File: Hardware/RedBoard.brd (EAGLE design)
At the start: 68.6 x 54.4 mm, 54 parts, among them IC1 FT232RLSSOP, IC2 LMV358, IC3 LM1117, J1 ICSP, J4 POWER_JACKSMD, Q1 MOSFET-PCHANNELSMD, U2 MIC5205, U3 ATMEGA328, Y1 16MHz

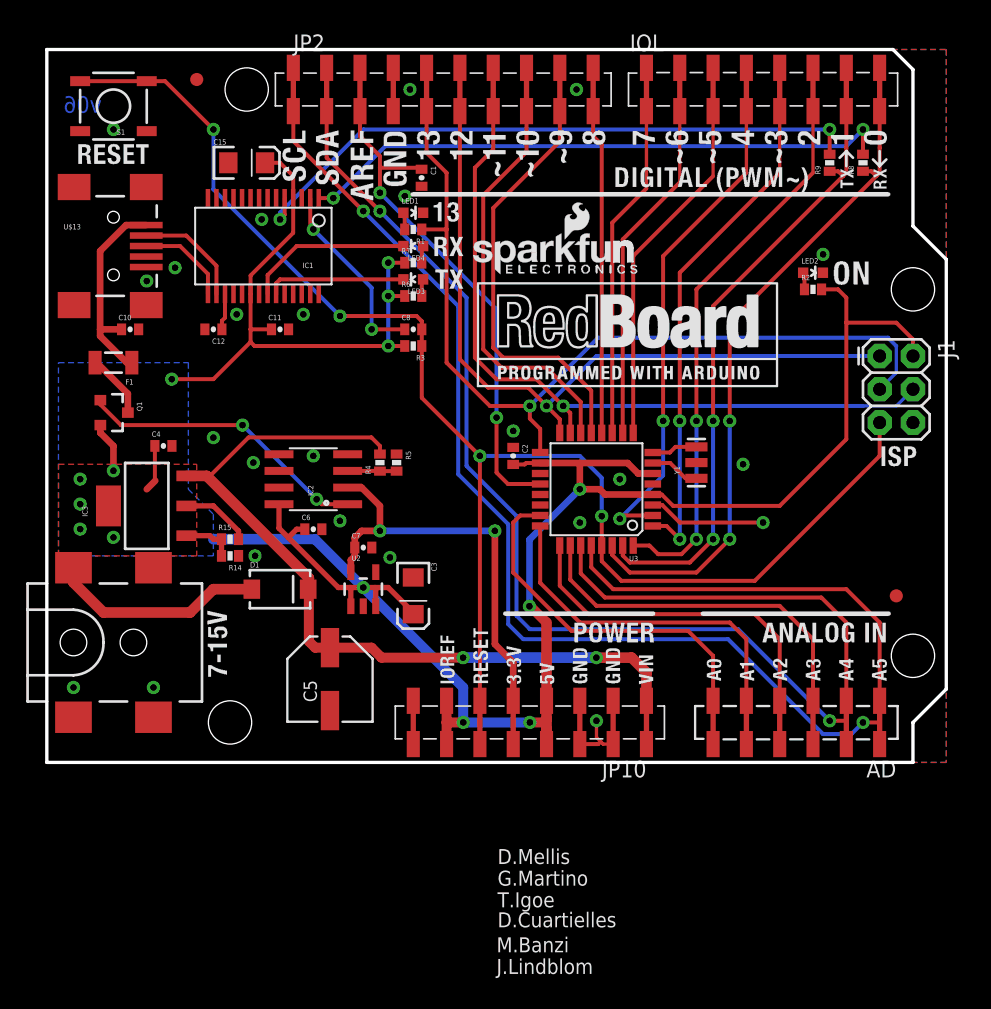
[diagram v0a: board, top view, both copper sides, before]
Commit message: New SMD ICSP header, logo, FT231X, power select
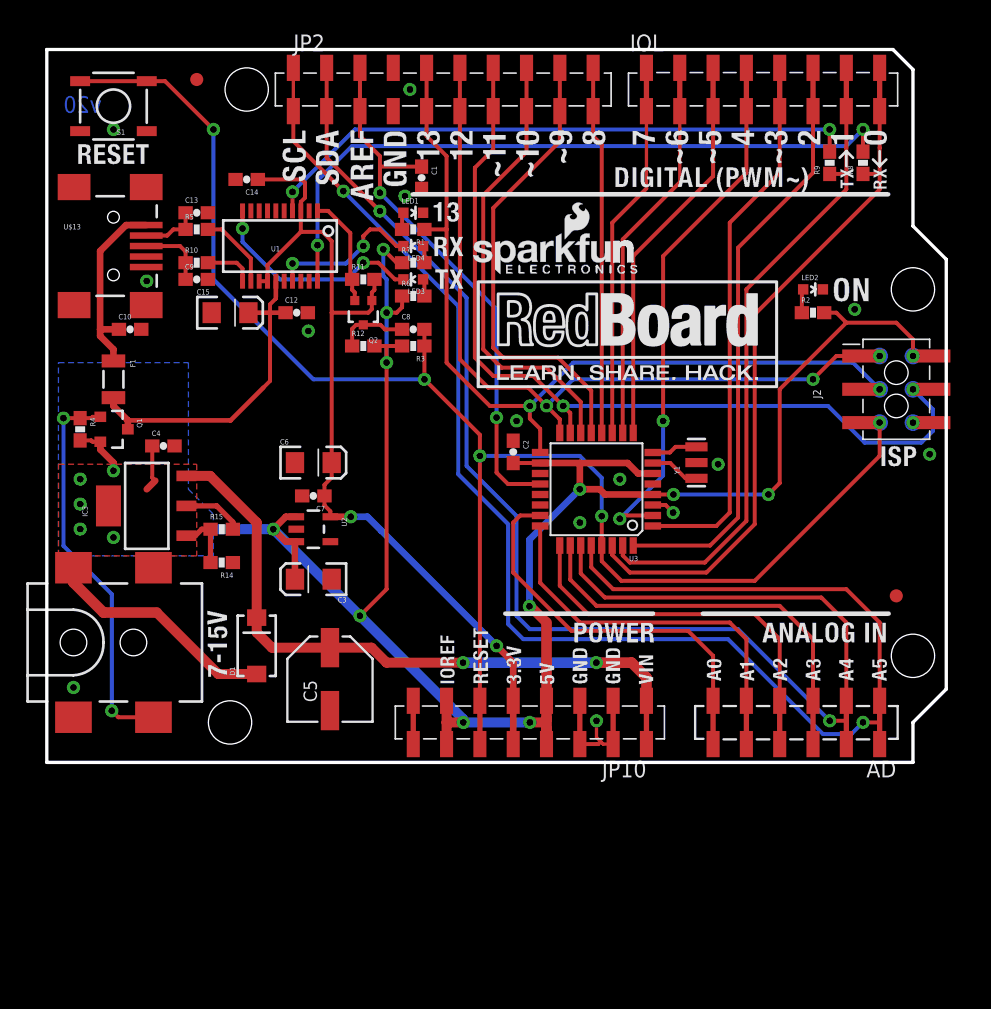
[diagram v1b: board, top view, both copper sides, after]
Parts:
- removed C11: 0.1uF, SparkFun-Capacitors:0402-CAP
- removed IC1: FT232RLSSOP, SparkFun-DigitalIC:SSOP28DB
- removed IC2: LMV358, SparkFun:SO08
- removed J1: ICSP, SparkFun:2X3
- removed U$15: CREATIVE_COMMONS, SparkFun:CREATIVE_COMMONS
- added C13, C9: 47pF, SparkFun-Capacitors:0603-CAP
- added C14: 0.1uF, SparkFun:0603-CAP
- added FRAME2: FRAME-LETTER, SparkFun-Aesthetics:CREATIVE_COMMONS
- added J2: AVR_SPI_PRG_6SMT_MALE, SparkFun-Connectors:2X3_SMT_POSTS
- added Q2: 2N7002PW, SparkFun-DiscreteSemi:SOT323
- added R10: 27, SparkFun-Resistors:0603-RES
- added R11, R12: 10k, SparkFun:0603-RES
- added TP1, TP2, TP3, TP4, TP5, TP6: TP-3x5, SparkFun-Passives:PAD.03X.05
- added U1: FT231XS, SparkFun-DigitalIC:SSOP20_L
- C1, C10, C12, C2, C4, C7, C8: device SparkFun:0402-CAP -> SparkFun:0603-CAP
- C6: value 0.1uF -> 10uF; device SparkFun:0402-CAP -> SparkFun:EIA3216
- JP2: value M10SMD -> M10SMD_COMBO
- Q1: value MOSFET-PCHANNELSMD -> ZXMP6A13FTA
- R1, R14, R15, R2, R3, R4, R6, R7, R8, R9: device SparkFun:0402-RES -> SparkFun:0603-RES
- R5: value 10k -> 27; device SparkFun:0402-RES -> SparkFun-Resistors:0603-RES
- moved R5 23.4 mm to (11.4, 40.6), turned to 0 degrees
- moved R4 23.0 mm to (2.54, 25.4), turned to 270 degrees
- moved C15 11.5 mm to (14.0, 34.3)
- moved C3 7.73 mm to (20.3, 14.0), turned to 180 degrees
- moved C12 6.48 mm to (19.1, 34.3), turned to 0 degrees
- moved U2 5.95 mm to (20.3, 17.8), turned to 270 degrees
- moved C7 5.48 mm to (20.3, 20.3), turned to 180 degrees
- moved C6 5.08 mm to (20.3, 22.9)
- moved D1 4.67 mm to (16.0, 8.89), turned to 90 degrees
- moved R2 1.78 mm to (58.4, 34.3)
- moved LED2 1.27 mm to (58.4, 36.1)
- moved Q1 1.27 mm to (5.08, 25.4)
- moved F1 1.27 mm to (5.08, 29.2), turned to 270 degrees
- moved R15 0.99 mm to (13.3, 17.8)
- moved R14 0.81 mm to (13.3, 15.2)
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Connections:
- removed net AD4: AD.5, JP2.2, JP2.2@2, U3.27
- removed net AD5: AD.6, JP2.1, JP2.1@2, U3.28
- removed net CMP: IC2.3, R4.1, R5.2
- removed net GATE_CMD: IC2.1, Q1.1
- removed net N$5: C12.1, IC1.17
- new net AD4/SDA: AD.5, JP2.2A, JP2.2B, U3.27
- new net AD5/SCL: AD.6, JP2.1A, JP2.1B, U3.28
- new net INSERT: J4.P$4, Q1.1, R4.1
- new net N$12: Q2.2, R11.1, U1.1
- new net N$6: R5.2, U1.12
- new net N$7: R10.2, U1.11
- net 3.3V: now also C14.1, C6.A, Q2.1, R11.2, U1.13, U1.14, U1.3; no longer IC2.2, JP10.5@2
- net 5V: now also J2.2, R12.2, R4.2, TP1.P$1; no longer C11.1, C15.A, C6.1, IC1.20, IC1.4, IC2.8, J1.2, JP10.4@2, JP10.7@2
- net AREF: now also JP2.3A, JP2.3B; no longer JP2.3, JP2.3@2
- net D+: now also C9.1, R10.1; no longer IC1.15
- net D-: now also C13.1, R5.1; no longer IC1.16
- net DTR: now also Q2.3, R12.1; no longer IC1.2
- net GND: now also C13.2, C14.2, C6.C, C9.2, J2.6, JP2.4A, JP2.4B, TP3.P$1, U1.16, U1.6; no longer C11.2, C6.2, IC1.18, IC1.21, IC1.25, IC1.26, IC1.7, IC2.4, IC2.5, IC2.6, J1.6, J4.P$4, JP10.2@2, JP10.3@2, JP2.4, JP2.4@2, R5.1
- net IO8: now also JP2.10A, JP2.10B; no longer JP2.10, JP2.10@2
- net IO9: now also JP2.9A, JP2.9B; no longer JP2.9, JP2.9@2
- net MISO: now also J2.1, JP2.6A, JP2.6B, TP4.P$1; no longer J1.1, JP2.6, JP2.6@2
- net MOSI: now also J2.4, JP2.7A, JP2.7B, TP2.P$1; no longer J1.4, JP2.7, JP2.7@2
- net RESET: now also J2.5, TP6.P$1; no longer J1.5, JP10.6@2
- net RXD: now also U1.4; no longer IC1.5
- net RXLED: now also U1.17; no longer IC1.22
- net SCK: now also J2.3, JP2.5A, JP2.5B, TP5.P$1; no longer J1.3, JP2.5, JP2.5@2
- net SS: now also JP2.8A, JP2.8B; no longer JP2.8, JP2.8@2
- net TXD: now also U1.20; no longer IC1.1
- net TXLED: now also U1.10; no longer IC1.23
- net USBVCC: now also C12.1, C15.A, U1.15
- net VIN: no longer JP10.1@2, R4.2
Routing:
- net AD5/SCL: track 0.00 -> 114.4 mm, vias 0 -> 2
- net AD5: track 114.4 -> 0.00 mm, vias 2 -> 0
- net AD4/SDA: track 0.00 -> 109.4 mm, vias 0 -> 2
- net AD4: track 109.4 -> 0.00 mm, vias 2 -> 0
- net 3.3V: track 35.4 -> 67.4 mm
- net INSERT: track 0.00 -> 30.1 mm, vias 0 -> 2
- net 5V: track 195.3 -> 169.6 mm, vias 14 -> 17
- net GATE_CMD: track 22.3 -> 0.00 mm, vias 2 -> 0
- net USBVCC: track 4.92 -> 25.6 mm
- net VIN: track 64.9 -> 51.4 mm
- net GND: track 16.7 -> 6.20 mm, vias 24 -> 15
- net DTR: track 14.5 -> 5.39 mm, vias 2 -> 0
- net N$12: track 0.00 -> 8.49 mm
- net MOSI: track 60.4 -> 68.0 mm, vias 1 -> 2
- net TXD: track 45.6 -> 52.6 mm
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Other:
- board text added: "v20"
- board text removed: "D.Cuartielles"
- board text removed: "D.Mellis"
- board text removed: "G.Martino"
- board text removed: "M.Banzi"
- board text removed: "R"
- board text removed: "T.Igoe"
- board text removed: "v06"

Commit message: Switch RX/TX labels, updating back logo
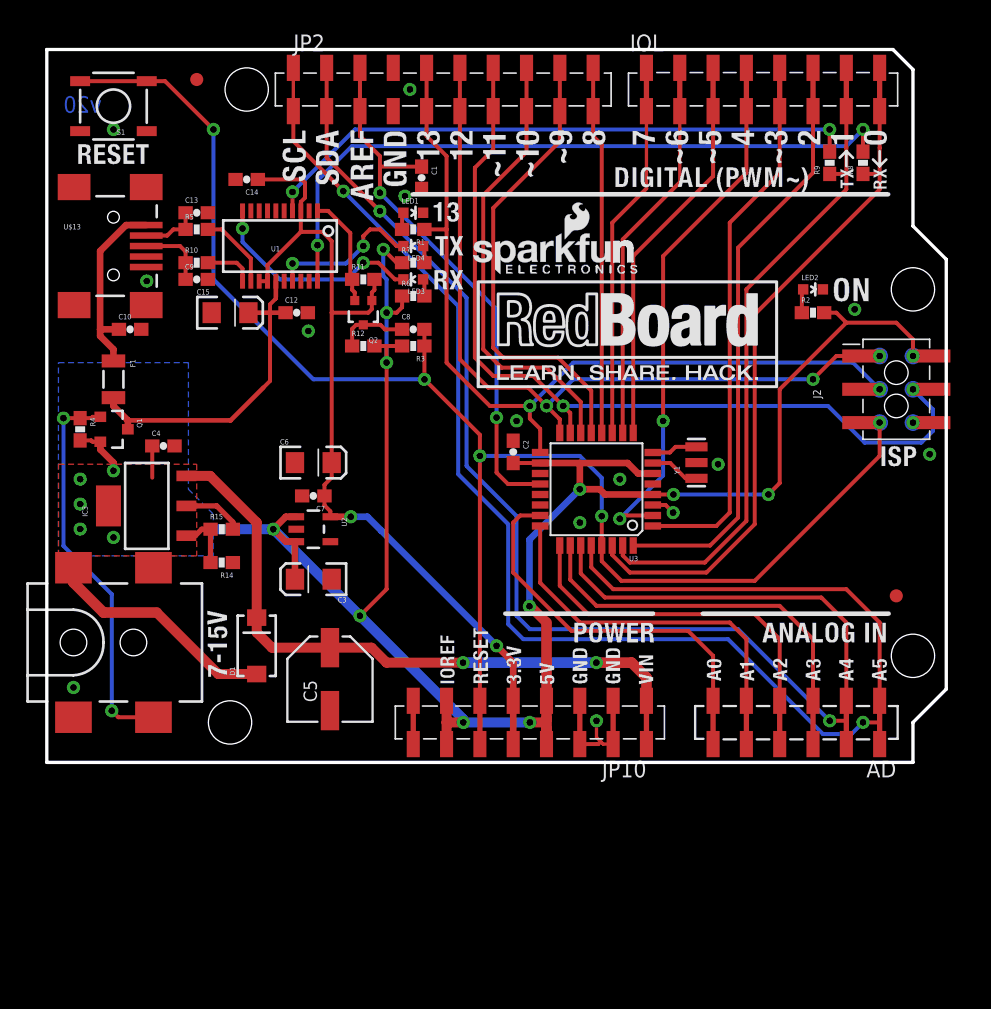
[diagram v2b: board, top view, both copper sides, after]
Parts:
- J2: value AVR_SPI_PRG_6SMT_MALE -> ICSP
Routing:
- net 5V: track 169.6 -> 168.3 mm

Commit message: LEDs to 1206; new barrel jack fp; moved 5V vreg
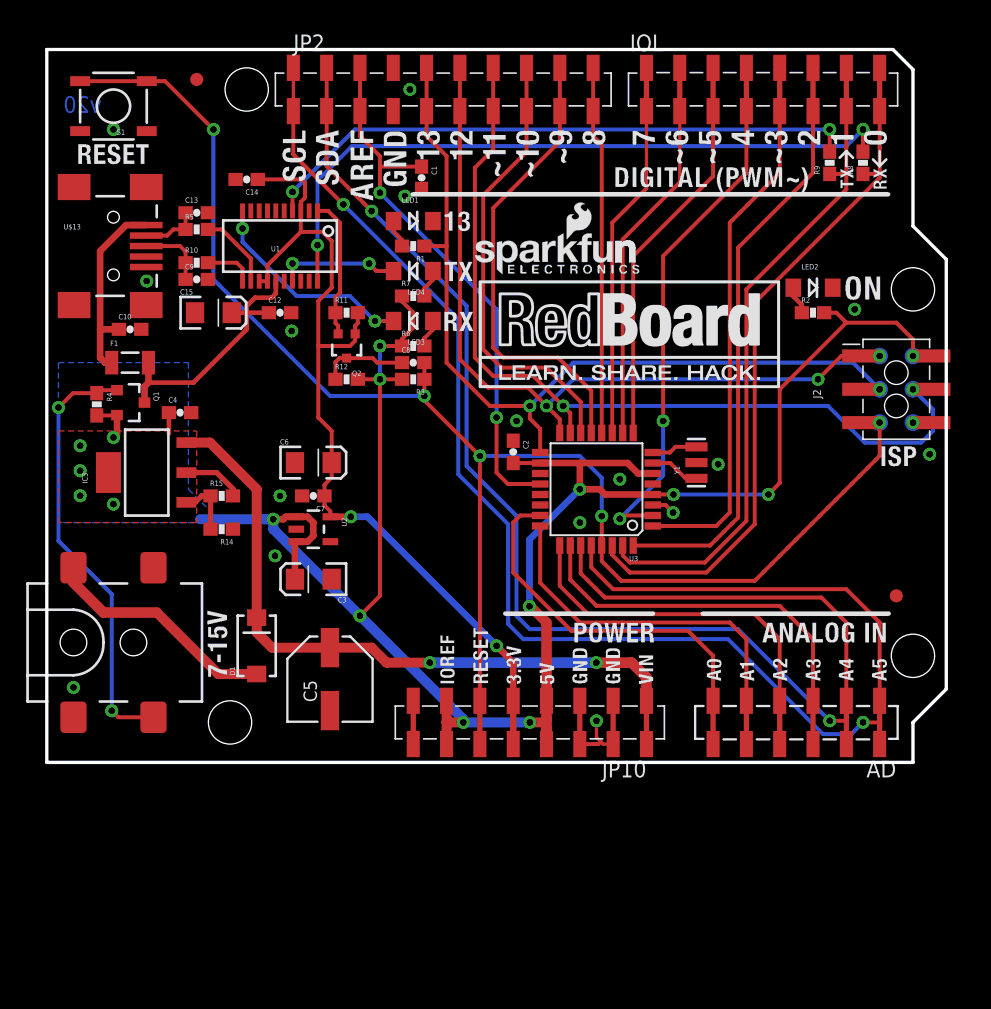
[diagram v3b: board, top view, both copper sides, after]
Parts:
- removed J4: POWER_JACKSMD, SparkFun:POWER_JACK_SMD
- added J1: POWER_JACKOVERPASTE_REDBOARD_0603, Testing:POWER_JACK_SMD_OVERPASTE_REDBOARD_0603
- LED1: value BLUE -> Blue; device SparkFun:LED-0603 -> SparkFun-LED:LED-1206-NO_SILK
- LED2: value GREEN -> Green; device SparkFun:LED-0603 -> SparkFun-LED:LED-1206-NO_SILK
- LED3: value RED -> Red; device SparkFun:LED-0603 -> SparkFun-LED:LED-1206-NO_SILK
- LED4: value YELLOW -> Yellow; device SparkFun:LED-0603 -> SparkFun-LED:LED-1206-NO_SILK
- moved R6 3.81 mm to (27.9, 31.8)
- moved LED3 3.17 mm to (27.9, 33.7), turned to 180 degrees
- moved C4 2.84 mm to (10.2, 26.7)
- moved Q2 2.84 mm to (22.9, 31.8)
- moved R11 2.84 mm to (22.9, 34.3)
- moved R12 2.84 mm to (22.9, 29.2)
- moved C8 2.54 mm to (27.9, 30.5)
- moved R14 2.54 mm to (13.3, 17.8)
- moved IC3 2.54 mm to (7.62, 22.1)
- moved R15 2.54 mm to (13.3, 20.3)
- moved R3 2.54 mm to (27.9, 29.2)
- moved R7 2.54 mm to (27.9, 35.6)
- moved Q1 2.40 mm to (6.35, 27.4)
- moved R4 2.29 mm to (3.81, 27.3)
- moved LED4 1.90 mm to (27.9, 37.5), turned to 180 degrees
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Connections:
- net GND: now also J1.GND; no longer J4.GND
- net INSERT: now also J1.P$4; no longer J4.P$4
- net PWRIN: now also J1.VIN0; no longer J4.VIN0
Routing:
- net USBVCC: track 25.6 -> 20.5 mm
- net 5V: track 168.3 -> 165.1 mm, vias 17 -> 16
- net INSERT: track 30.1 -> 33.2 mm
- net RXLED: track 11.9 -> 9.29 mm
- net VIN: track 51.4 -> 54.0 mm
- net N$12: track 8.49 -> 10.8 mm
- net RESET: track 121.8 -> 119.8 mm
- net DTR: track 5.39 -> 6.66 mm
- net N$10: track 1.45 -> 2.17 mm
- net N$1: track 1.45 -> 2.17 mm
- net N$8: track 1.45 -> 2.17 mm
- net 3.3V: track 67.4 -> 67.9 mm
- net GND: vias 15 -> 17
